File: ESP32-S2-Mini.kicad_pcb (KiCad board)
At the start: 2 copper layers, 25.4 x 54 mm, 14 parts, among them J1 Conn_01x21, J2 Conn_01x21, J3 Conn_02x03_Odd_Even, J4 Conn_02x05_Odd_Even, U1 TC2117-3.3VDBTR, U2 ESP32-S2-MINI-1

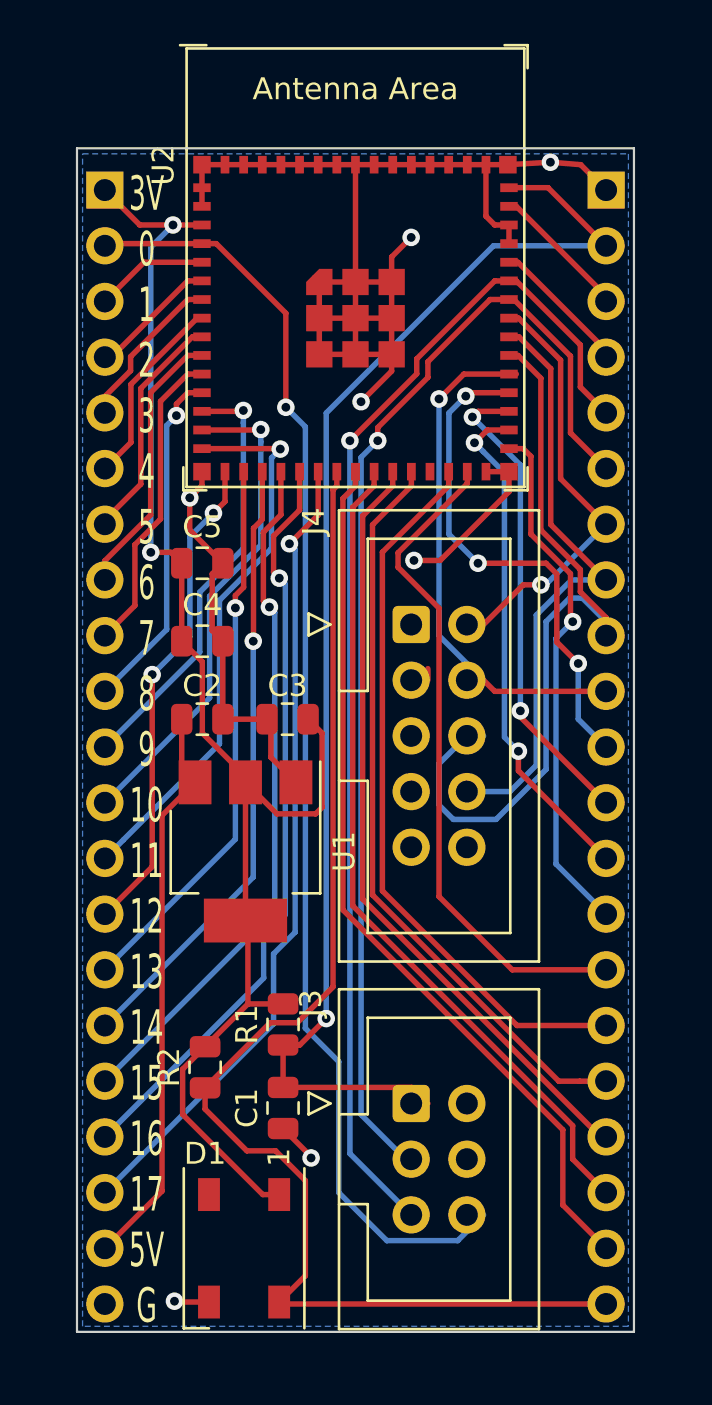
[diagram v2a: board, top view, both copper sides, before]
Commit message: Fixed labels on right 21-pin connector block
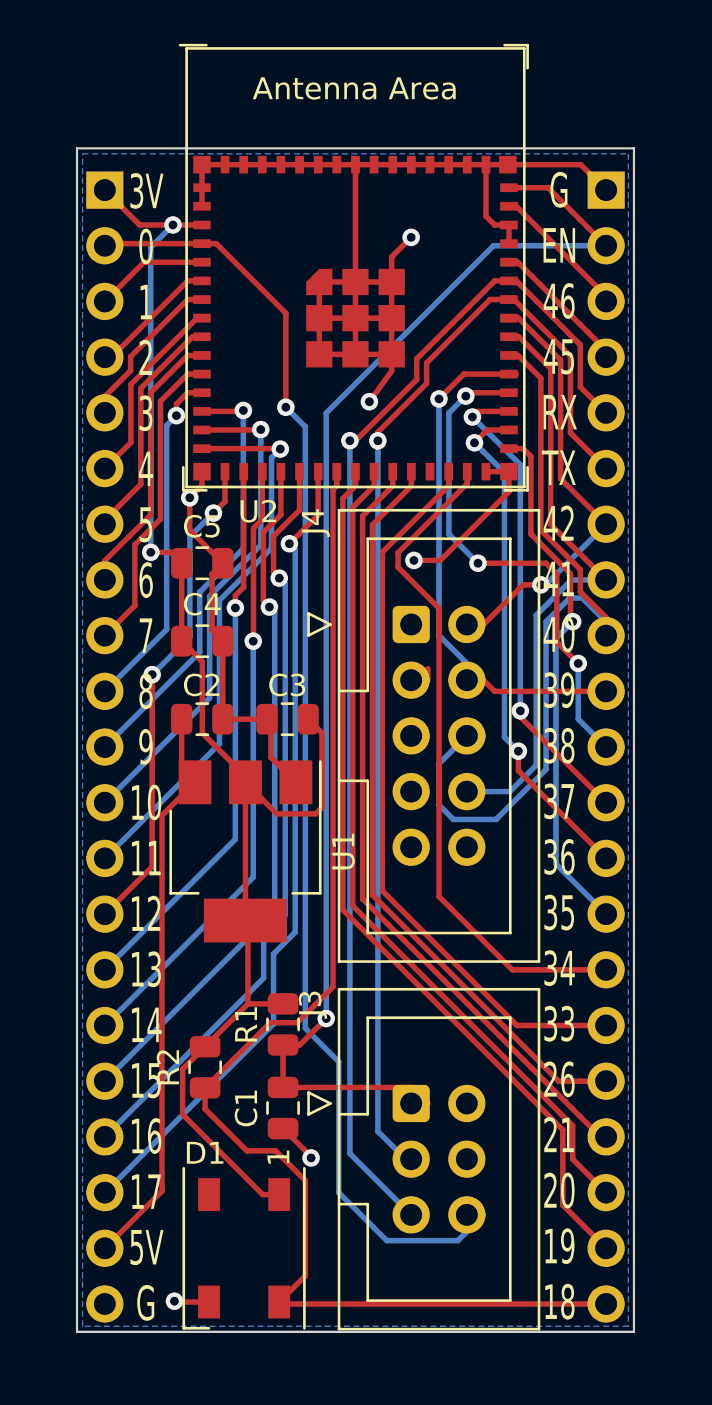
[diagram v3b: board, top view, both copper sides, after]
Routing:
- net /TX: track 53.0 -> 52.4 mm
- net GND: track 85.4 -> 85.1 mm, vias 7 -> 6
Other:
- board text added: "G EN 46 45 RX TX 42 41 40 39 38 37 36 35 34 33 26 21 20 19 18"
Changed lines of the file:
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@@
   (general
     (thickness 1.6)
-    (drawings 5)
-    (tracks 388)
+    (drawings 6)
+    (tracks 387)
     (zones 0)
     (modules 14)
@@
     (tags ESP32-S2)
     (attr smd)
-    (fp_text reference U2 (at -8.763 -6.985 90) (layer F.SilkS)
+    (fp_text reference U2 (at -4.4196 8.8392) (layer F.SilkS)
       (effects (font (size 1 1) (thickness 0.15)))
     )
@@
     (descr "Through hole straight pin header, 1x21, 2.54mm pitch, single row")
     (tags "Through hole pin header THT 1x21 2.54mm single row")
-    (fp_text reference J2 (at 0 1.905) (layer B.SilkS)
+    (fp_text reference J2 (at 2.54 0.762 90) (layer B.SilkS)
       (effects (font (size 1 1) (thickness 0.15)) (justify mirror))
     )
@@
     (descr "Through hole straight pin header, 1x21, 2.54mm pitch, single row")
     (tags "Through hole pin header THT 1x21 2.54mm single row")
-    (fp_text reference J1 (at 0 1.905) (layer B.SilkS)
+    (fp_text reference J1 (at -2.286 0.635 90) (layer B.SilkS)
       (effects (font (size 1 1) (thickness 0.15)) (justify mirror))
     )
@@
     )
   )
-  (gr_text "3V\n0\n1\n2\n3\n4\n5\n6\n7\n8\n9\n10\n11\n12\n13\n14\n15\n16\n17\n5V\nG" (at 189.865 96.647) (layer F.SilkS)
+  (gr_text "G\nEN\n46\n45\nRX\nTX\n42\n41\n40\n39\n38\n37\n36\n35\n34\n33\n26\n21\n20\n19\n18" (at 208.6864 96.52) (layer F.SilkS)
+    (effects (font (size 1.5748 0.889) (thickness 0.1778)))
+  )
+  (gr_text "3V\n0\n1\n2\n3\n4\n5\n6\n7\n8\n9\n10\n11\n12\n13\n14\n15\n16\n17\n5V\nG" (at 189.8396 96.5708) (layer F.SilkS)
     (effects (font (size 1.5748 0.889) (thickness 0.1778)))
   )
@@
   (segment (start 205.34 69.962) (end 205.34 72.312) (width 0.25) (layer F.Cu) (net 2))
   (segment (start 206.39 72.712) (end 206.39 73.562) (width 0.25) (layer F.Cu) (net 2))
-  (segment (start 209.662 69.962) (end 210.82 71.12) (width 0.25) (layer F.Cu) (net 2))
-  (segment (start 206.34 69.962) (end 208.28 69.85) (width 0.25) (layer F.Cu) (net 2))
-  (segment (start 208.28 69.85) (end 209.662 69.962) (width 0.25) (layer F.Cu) (net 2))
-  (via (at 208.28 69.85) (size 0.8) (drill 0.4) (layers F.Cu B.Cu) (net 2))
   (via (at 191.135 121.793) (size 0.8) (drill 0.4) (layers F.Cu B.Cu) (net 2))
   (segment (start 191.172 121.83) (end 191.135 121.793) (width 0.25) (layer F.Cu) (net 2))
@@
   (segment (start 192.39 83.962) (end 192.39 84.597) (width 0.25) (layer F.Cu) (net 2))
   (segment (start 192.39 84.597) (end 191.8335 85.1535) (width 0.25) (layer F.Cu) (net 2))
-  (segment (start 201.04 78.612) (end 201.04 79.376) (width 0.25) (layer F.Cu) (net 2))
-  (via (at 199.644 80.772) (size 0.8) (drill 0.4) (layers F.Cu B.Cu) (net 2))
-  (segment (start 201.04 79.376) (end 199.644 80.772) (width 0.25) (layer F.Cu) (net 2))
   (via (at 202.057 88.011) (size 0.8) (drill 0.4) (layers F.Cu B.Cu) (net 2))
   (segment (start 206.39 83.962) (end 206.39 84.878687) (width 0.25) (layer F.Cu) (net 2))
   (segment (start 203.257687 88.011) (end 202.057 88.011) (width 0.25) (layer F.Cu) (net 2))
   (segment (start 206.39 84.878687) (end 203.257687 88.011) (width 0.25) (layer F.Cu) (net 2))
+  (segment (start 201.04 79.376) (end 201.04 78.612) (width 0.25) (layer F.Cu) (net 2))
+  (segment (start 200.025 80.772) (end 201.04 79.376) (width 0.25) (layer F.Cu) (net 2))
+  (via (at 200.025 80.772) (size 0.8) (drill 0.4) (layers F.Cu B.Cu) (net 2))
+  (segment (start 209.662 69.962) (end 210.82 71.12) (width 0.25) (layer F.Cu) (net 2))
+  (segment (start 206.34 69.962) (end 209.662 69.962) (width 0.25) (layer F.Cu) (net 2))
   (segment (start 190.569009 99.636991) (end 192.0735 98.1325) (width 0.25) (layer F.Cu) (net 3))
   (segment (start 190.569009 116.770991) (end 190.569009 99.636991) (width 0.25) (layer F.Cu) (net 3))
@@
   (segment (start 204.333 79.512) (end 203.2 80.645) (width 0.25) (layer F.Cu) (net 34))
   (segment (start 206.39 79.512) (end 204.333 79.512) (width 0.25) (layer F.Cu) (net 34))
-  (segment (start 205.232 93.472) (end 205.74 93.98) (width 0.25) (layer F.Cu) (net 34))
-  (segment (start 205.74 93.98) (end 209.617919 93.98) (width 0.25) (layer F.Cu) (net 34))
-  (segment (start 209.617919 93.98) (end 210.82 93.98) (width 0.25) (layer F.Cu) (net 34))
   (segment (start 205.232 93.472) (end 205.105 93.345) (width 0.25) (layer B.Cu) (net 34))
   (segment (start 203.2 91.44) (end 205.232 93.472) (width 0.25) (layer B.Cu) (net 34))
   (segment (start 203.2 80.645) (end 203.2 91.44) (width 0.25) (layer B.Cu) (net 34))
+  (segment (start 209.617919 93.98) (end 210.82 93.98) (width 0.25) (layer F.Cu) (net 34))
+  (segment (start 205.74 93.98) (end 209.617919 93.98) (width 0.25) (layer F.Cu) (net 34))
+  (segment (start 205.232 93.472) (end 205.74 93.98) (width 0.25) (layer F.Cu) (net 34))
   (segment (start 210.82 90.618174) (end 210.82 91.44) (width 0.25) (layer F.Cu) (net 35))
   (segment (start 209.644999 89.443173) (end 210.82 90.618174) (width 0.25) (layer F.Cu) (net 35))
@@
   (segment (start 206.614035 76.112) (end 209.19499 78.692955) (width 0.25) (layer F.Cu) (net 38))
   (segment (start 206.39 76.112) (end 206.614035 76.112) (width 0.25) (layer F.Cu) (net 38))
-  (via (at 200.406 82.55) (size 0.8) (drill 0.4) (layers F.Cu B.Cu) (net 38))
-  (segment (start 202.692 79.663999) (end 200.406 81.949999) (width 0.25) (layer F.Cu) (net 38))
-  (segment (start 200.406 81.949999) (end 200.406 82.55) (width 0.25) (layer F.Cu) (net 38))
-  (segment (start 202.692 78.95) (end 202.692 79.663999) (width 0.25) (layer F.Cu) (net 38))
-  (segment (start 205.53 76.112) (end 202.692 78.95) (width 0.25) (layer F.Cu) (net 38))
+  (segment (start 201.676 115.316) (end 200.41066 114.05066) (width 0.25) (layer B.Cu) (net 38))
+  (segment (start 202.634011 79.9424) (end 200.41066 82.16575) (width 0.25) (layer F.Cu) (net 38))
+  (segment (start 200.41066 82.16575) (end 200.41066 82.55466) (width 0.25) (layer F.Cu) (net 38))
+  (segment (start 200.41066 83.120345) (end 200.41066 82.55466) (width 0.25) (layer B.Cu) (net 38))
+  (via (at 200.41066 82.55466) (size 0.8) (drill 0.4) (layers F.Cu B.Cu) (net 38))
   (segment (start 206.39 76.112) (end 205.53 76.112) (width 0.25) (layer F.Cu) (net 38))
-  (segment (start 199.644 113.284) (end 201.676 115.316) (width 0.25) (layer B.Cu) (net 38))
-  (segment (start 199.644 83.312) (end 199.644 113.284) (width 0.25) (layer B.Cu) (net 38))
-  (segment (start 200.406 82.55) (end 199.644 83.312) (width 0.25) (layer B.Cu) (net 38))
+  (segment (start 205.53 76.112) (end 202.634011 79.007989) (width 0.25) (layer F.Cu) (net 38))
+  (segment (start 200.41066 114.05066) (end 200.41066 83.120345) (width 0.25) (layer B.Cu) (net 38))
+  (segment (start 202.634011 79.007989) (end 202.634011 79.9424) (width 0.25) (layer F.Cu) (net 38))
   (segment (start 209.644999 80.104999) (end 210.82 81.28) (width 0.25) (layer F.Cu) (net 39))
   (segment (start 206.725002 75.262) (end 209.644999 78.181997) (width 0.25) (layer F.Cu) (net 39))
@@
   (segment (start 206.39 75.262) (end 206.725002 75.262) (width 0.25) (layer F.Cu) (net 39))
   (via (at 199.136 82.55) (size 0.8) (drill 0.4) (layers F.Cu B.Cu) (net 39))
-  (segment (start 202.184 79.502) (end 199.136 82.55) (width 0.25) (layer F.Cu) (net 39))
-  (segment (start 202.184 78.818) (end 202.184 79.502) (width 0.25) (layer F.Cu) (net 39))
-  (segment (start 205.74 75.262) (end 202.184 78.818) (width 0.25) (layer F.Cu) (net 39))
-  (segment (start 206.39 75.262) (end 205.74 75.262) (width 0.25) (layer F.Cu) (net 39))
   (segment (start 199.136 115.062) (end 201.93 117.856) (width 0.25) (layer B.Cu) (net 39))
   (segment (start 199.136 82.55) (end 199.136 115.062) (width 0.25) (layer B.Cu) (net 39))
+  (segment (start 199.39 82.55) (end 199.136 82.55) (width 0.25) (layer F.Cu) (net 39))
+  (segment (start 202.184 79.756) (end 199.39 82.55) (width 0.25) (layer F.Cu) (net 39))
+  (segment (start 202.184 78.818) (end 202.184 79.756) (width 0.25) (layer F.Cu) (net 39))
+  (segment (start 206.39 75.262) (end 205.74 75.262) (width 0.25) (layer F.Cu) (net 39))
+  (segment (start 205.74 75.262) (end 202.184 78.818) (width 0.25) (layer F.Cu) (net 39))
   (segment (start 210.82 78.432999) (end 210.82 78.74) (width 0.25) (layer F.Cu) (net 40))
   (segment (start 206.799001 74.412) (end 210.82 78.432999) (width 0.25) (layer F.Cu) (net 40))
